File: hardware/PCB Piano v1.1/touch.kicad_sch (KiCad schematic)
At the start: 74 parts, among them U10 MTCH2120-V/SO, U5 MTCH2120-V/SO

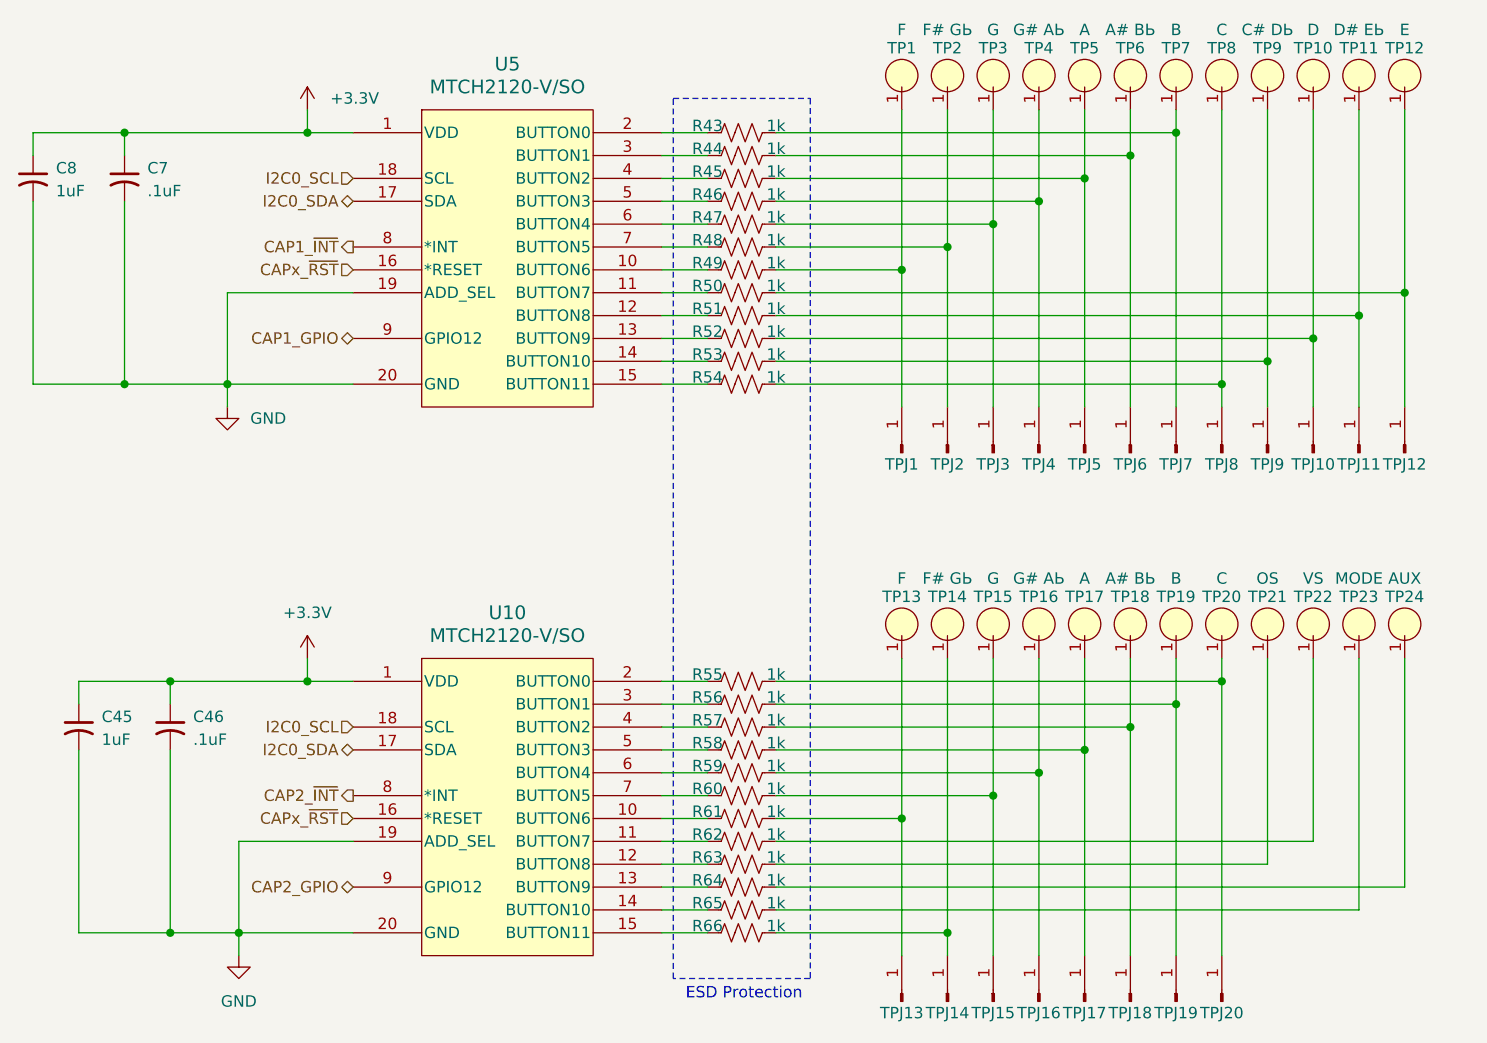
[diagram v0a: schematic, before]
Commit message: Firmware architecture complete - PCB revision with new charger.
Firmware Architecture Complete

- Added MP2724 charger driver
- Added TLV320DAC3100 driver
- Added MTCH2120 touch driver
- Added PCA9685 driver
- Added DotStar driver
- Added rotary encoder driver
- Added touch and LED maps
- Added control/audio/voice managers
- Added audio command queue
- Added Core1 audio architecture
- Added status LED system
- Added LED animation framework

Changes hardware schematic and PCB to accommodate a newer-style USB-C sink battery charger chip and USB data MUX to protect MCU while powered off.
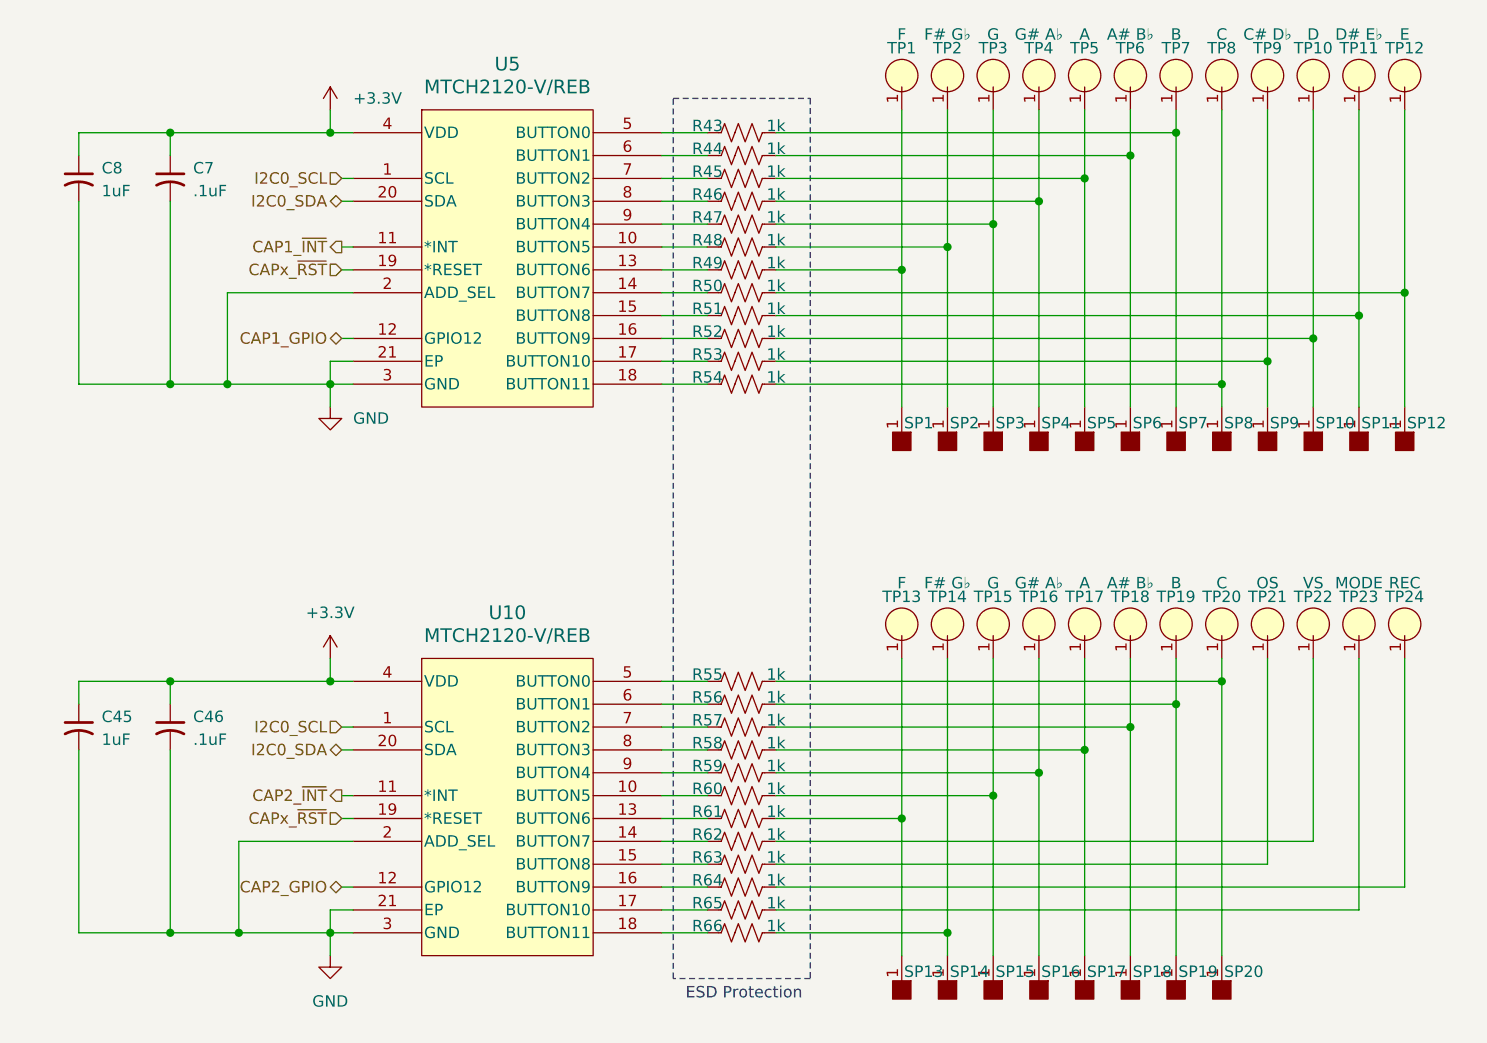
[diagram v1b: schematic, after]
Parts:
- removed TPJ1, TPJ13: F, PCBPiano_Footprints:Terminal_SMD_.250in, symbol Connector:Conn_01x01_Pin
- removed TPJ10: D, PCBPiano_Footprints:Terminal_SMD_.250in, symbol Connector:Conn_01x01_Pin
- removed TPJ11: D# Eb, PCBPiano_Footprints:Terminal_SMD_.250in, symbol Connector:Conn_01x01_Pin
- removed TPJ12: E, PCBPiano_Footprints:Terminal_SMD_.250in, symbol Connector:Conn_01x01_Pin
- removed TPJ14, TPJ2: F# Gb, PCBPiano_Footprints:Terminal_SMD_.250in, symbol Connector:Conn_01x01_Pin
- removed TPJ15, TPJ3: G, PCBPiano_Footprints:Terminal_SMD_.250in, symbol Connector:Conn_01x01_Pin
- removed TPJ16, TPJ4: G# Ab, PCBPiano_Footprints:Terminal_SMD_.250in, symbol Connector:Conn_01x01_Pin
- removed TPJ17, TPJ5: A, PCBPiano_Footprints:Terminal_SMD_.250in, symbol Connector:Conn_01x01_Pin
- removed TPJ18, TPJ6: A# Bb, PCBPiano_Footprints:Terminal_SMD_.250in, symbol Connector:Conn_01x01_Pin
- removed TPJ19, TPJ7: B, PCBPiano_Footprints:Terminal_SMD_.250in, symbol Connector:Conn_01x01_Pin
- removed TPJ20, TPJ8: C, PCBPiano_Footprints:Terminal_SMD_.250in, symbol Connector:Conn_01x01_Pin
- removed TPJ9: C# Db, PCBPiano_Footprints:Terminal_SMD_.250in, symbol Connector:Conn_01x01_Pin
- added SP1, SP10, SP11, SP12, SP13, SP14, SP15, SP16, SP17, SP18, SP19, SP2, SP20, SP3, SP4, SP5, SP6, SP7, SP8, SP9: (no value), PCBPiano_Footprints:Pad_Solder_SMT_5x7mm, symbol PCB_Piano_Symbols:Pad_Solder
- TP1, TP13: value F -> (none); Note (none) -> F
- TP10: value D -> (none); Note (none) -> D
- TP11: value D# EЬ -> (none); Note (none) -> D# E♭
- TP12: value E -> (none); Note (none) -> E
- TP14, TP2: value F# GЬ -> (none); Note (none) -> F# G♭
- TP15, TP3: value G -> (none); Note (none) -> G
- TP16, TP4: value G# AЬ -> (none); Note (none) -> G# A♭
- TP17, TP5: value A -> (none); Note (none) -> A
- TP18, TP6: value A# BЬ -> (none); Note (none) -> A# B♭
- TP19, TP7: value B -> (none); Note (none) -> B
- TP20, TP8: value C -> (none); Note (none) -> C
- TP21: value OS -> (none); Note (none) -> OS
- TP22: value VS -> (none); Note (none) -> VS
- TP23: value MODE -> (none); Note (none) -> MODE
- TP24: value AUX -> (none); Note (none) -> REC
- TP9: value C# DЬ -> (none); Note (none) -> C# D♭
- U10, U5: value MTCH2120-V/SO -> MTCH2120-V/REB; footprint Package_SO:SOIC-20W_7.5x12.8mm_P1.27mm -> Package_DFN_QFN:VQFN-20-1EP_3x3mm_P0.4mm_EP1.7x1.7mm; symbol PCB Piano Symbols:MTCH2120-V_SO -> PCB Piano Symbols:MTCH2120-V/REB
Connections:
- net +3.3V: now also U10.4 (VDD), U5.4 (VDD); no longer U10.1 (VDD), U5.1 (VDD)
- net CAP1_GPIO: now also U5.12 (GPIO12); no longer U5.9 (GPIO12)
- net CAP1_~{INT}: now also U5.11 (*INT); no longer U5.8 (*INT)
- net CAP2_GPIO: now also U10.12 (GPIO12); no longer U10.9 (GPIO12)
- net CAP2_~{INT}: now also U10.11 (*INT); no longer U10.8 (*INT)
- net CAPx_~{RST}: now also U10.19 (*RESET), U5.19 (*RESET); no longer U10.16 (*RESET), U5.16 (*RESET)
- net GND: now also U10.2 (ADD_SEL), U10.21 (EP), U10.3 (GND), U5.2 (ADD_SEL), U5.21 (EP), U5.3 (GND); no longer U10.19 (ADD_SEL), U10.20 (GND), U5.19 (ADD_SEL), U5.20 (GND)
- net I2C0_SCL: now also U10.1 (SCL), U5.1 (SCL); no longer U10.18 (SCL), U5.18 (SCL)
- net I2C0_SDA: now also U10.20 (SDA), U5.20 (SDA); no longer U10.17 (SDA), U5.17 (SDA)
- net at R53.1: now also U5.17 (BUTTON10); no longer U5.14 (BUTTON10)
- net at R53.2, TP9.1: now also SP9.1
- net at R60.2, TP15.1: now also SP15.1
- net at R44.2, TP6.1: now also SP6.1
- net at R50.1: now also U5.14 (BUTTON7); no longer U5.11 (BUTTON7)
- net at R50.2, TP12.1: now also SP12.1
- net at R64.1: now also U10.16 (BUTTON9); no longer U10.13 (BUTTON9)
- net at R46.2, TP4.1: now also SP4.1
- net at R43.2, TP7.1: now also SP7.1
- net at U10.10 (BUTTON5): now also R60.1; no longer R61.1
- net at R62.1: now also U10.14 (BUTTON7); no longer U10.11 (BUTTON7)
- net at R63.1: now also U10.15 (BUTTON8); no longer U10.12 (BUTTON8)
- net at R65.1: now also U10.17 (BUTTON10); no longer U10.14 (BUTTON10)
- net at R66.1: now also U10.18 (BUTTON11); no longer U10.15 (BUTTON11)
- net at R55.1: now also U10.5 (BUTTON0); no longer U10.2 (BUTTON0)
- net at R56.1: now also U10.6 (BUTTON1); no longer U10.3 (BUTTON1)
- net at R57.1: now also U10.7 (BUTTON2); no longer U10.4 (BUTTON2)
- net at R58.1: now also U10.8 (BUTTON3); no longer U10.5 (BUTTON3)
- net at R59.1: now also U10.9 (BUTTON4); no longer U10.6 (BUTTON4)
- net at R61.2, TP13.1: now also SP13.1
- net at R54.1: now also U5.18 (BUTTON11); no longer U5.15 (BUTTON11)
- net at R54.2, TP8.1: now also SP8.1
- net at R58.2, TP17.1: now also SP17.1
- net at R57.2, TP18.1: now also SP18.1
- net at R45.2, TP5.1: now also SP5.1
- net at R56.2, TP19.1: now also SP19.1
- net at R52.2, TP10.1: now also SP10.1
- net at R49.2, TP1.1: now also SP1.1
- net at R45.1: now also U5.7 (BUTTON2); no longer U5.4 (BUTTON2)
- net at U5.10 (BUTTON5): now also R48.1; no longer R49.1
- net at R51.1: now also U5.15 (BUTTON8); no longer U5.12 (BUTTON8)
- net at U5.13 (BUTTON6): now also R49.1; no longer R52.1
- net at R43.1: now also U5.5 (BUTTON0); no longer U5.2 (BUTTON0)
- net at R44.1: now also U5.6 (BUTTON1); no longer U5.3 (BUTTON1)
- net at R46.1: now also U5.8 (BUTTON3); no longer U5.5 (BUTTON3)
- net at R47.1: now also U5.9 (BUTTON4); no longer U5.6 (BUTTON4)
- net at R47.2, TP3.1: now also SP3.1
- net at R59.2, TP16.1: now also SP16.1
- net at R55.2, TP20.1: now also SP20.1
- net at R66.2, TP14.1: now also SP14.1
- net at R51.2, TP11.1: now also SP11.1
- net at R48.2, TP2.1: now also SP2.1
- new net: R61.1, U10.13 (BUTTON6)
- new net: R52.1, U5.16 (BUTTON9)
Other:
- moved on the sheet: C7, C8

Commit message: PCB Finalized and Ordered. Firmware near completion.
PCB Finalized and Ordered. Final revisions included fixing bugs on some peripheral chips. Also added an RTC circuit after realizing the SD card could benefit from adding file timestamps.

Firmware near completion. Still need to finalize some SD card operations. Synth audio core is finished and all the board peripheral chip drivers were completed.
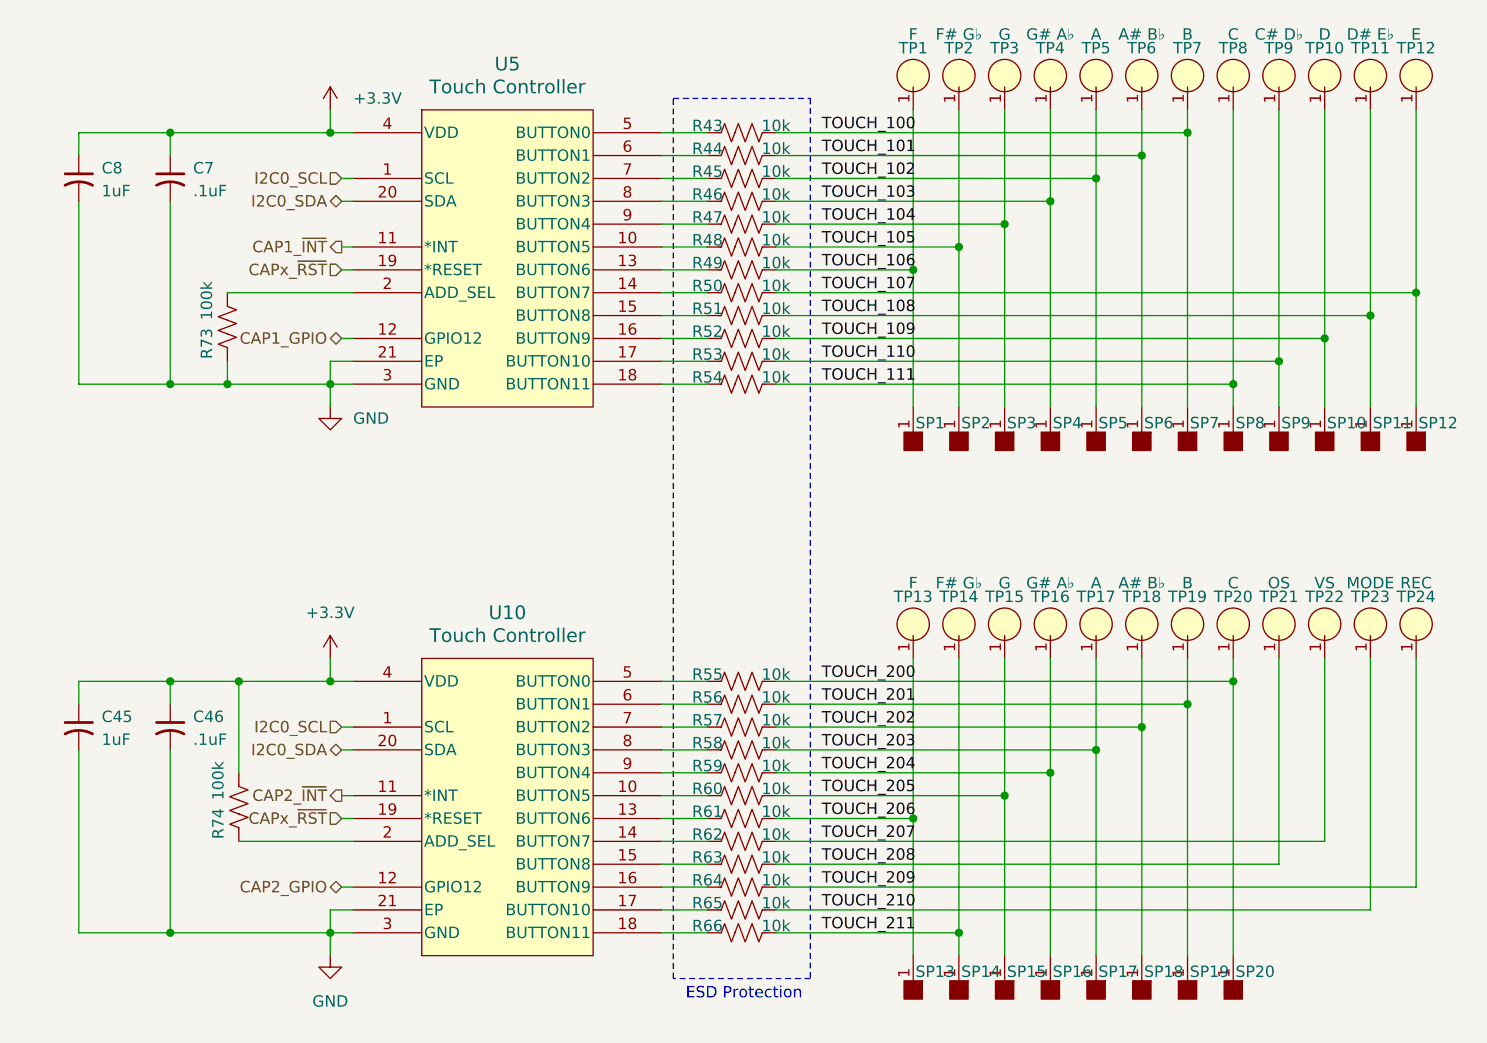
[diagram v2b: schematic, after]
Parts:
- added R73, R74: 100k, Resistor_SMD:R_0603_1608Metric, symbol Device:R_US
- C45, C8: DigiKey_Part_Number (none) -> 1276-1184-1-ND; Manufacturer Part Number (none) -> CL10B105KA8NNNC; Volt Rating (none) -> 10V
- C46, C7: DigiKey_Part_Number (none) -> 1276-1935-2-ND; Manufacturer Part Number (none) -> CL10B104KB8NNWC; Volt Rating (none) -> 10V
- R43, R44, R45, R46, R47, R48, R49, R50, R51, R52, R53, R54, R55, R56, R57, R58, R59, R60, R61, R62, R63, R64, R65, R66: value 1k -> 10k
- TP1, TP10, TP11, TP12, TP13, TP14, TP15, TP16, TP17, TP18, TP19, TP2, TP20, TP21, TP22, TP23, TP24, TP3, TP4, TP5, TP6, TP7, TP8, TP9: now left out of the parts list
- U10, U5: value MTCH2120-V/REB -> Touch Controller; DigiKey_Part_Number (none) -> MTCH2120-V/REB; Manufacturer Part Number (none) -> MTCH2120-V/REB
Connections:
- net +3.3V: now also R74.1
- net GND: now also R73.2; no longer U10.2 (ADD_SEL), U5.2 (ADD_SEL)
- net TOUCH_110: now reaches R53.2, SP9.1, TP9.1
- net TOUCH_101: now reaches R44.2, SP6.1, TP6.1
- net TOUCH_210: now reaches R65.2, TP23.1
- net TOUCH_104: now reaches R47.2, SP3.1, TP3.1
- net TOUCH_109: now reaches R52.2, SP10.1, TP10.1
- net TOUCH_107: now reaches R50.2, SP12.1, TP12.1
- net TOUCH_209: now reaches R64.2, TP24.1
- net TOUCH_207: now reaches R62.2, TP22.1
- net TOUCH_203: now reaches R58.2, SP17.1, TP17.1
- net TOUCH_103: now reaches R46.2, SP4.1, TP4.1
- net TOUCH_111: now reaches R54.2, SP8.1, TP8.1
- net TOUCH_202: now reaches R57.2, SP18.1, TP18.1
- net TOUCH_102: now reaches R45.2, SP5.1, TP5.1
- net TOUCH_200: now reaches R55.2, SP20.1, TP20.1
- net TOUCH_206: now reaches R61.2, SP13.1, TP13.1
- net TOUCH_205: now reaches R60.2, SP15.1, TP15.1
- net TOUCH_201: now reaches R56.2, SP19.1, TP19.1
- net TOUCH_208: now reaches R63.2, TP21.1
- net TOUCH_105: now reaches R48.2, SP2.1, TP2.1
- net TOUCH_204: now reaches R59.2, SP16.1, TP16.1
- net TOUCH_106: now reaches R49.2, SP1.1, TP1.1
- net TOUCH_108: now reaches R51.2, SP11.1, TP11.1
- net TOUCH_211: now reaches R66.2, SP14.1, TP14.1
- net TOUCH_100: now reaches R43.2, SP7.1, TP7.1
- new net: R74.2, U10.2 (ADD_SEL)
- new net: R73.1, U5.2 (ADD_SEL)
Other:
- moved on the sheet: SP1, SP10, SP11, SP12, SP13, SP14, SP15, SP16, SP17, SP18, SP19, SP2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
